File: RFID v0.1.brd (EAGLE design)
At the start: 87 x 53.3 mm, 32 parts, among them K1 G5LE, Q1 XTAL 16MHz, T1 BC817-40, U1 ARDUINOSPI-REFRENCE, U2 POWER-POD 5V0, U3 ATMEGA328P-MU, U4 POWER-POD 3V3

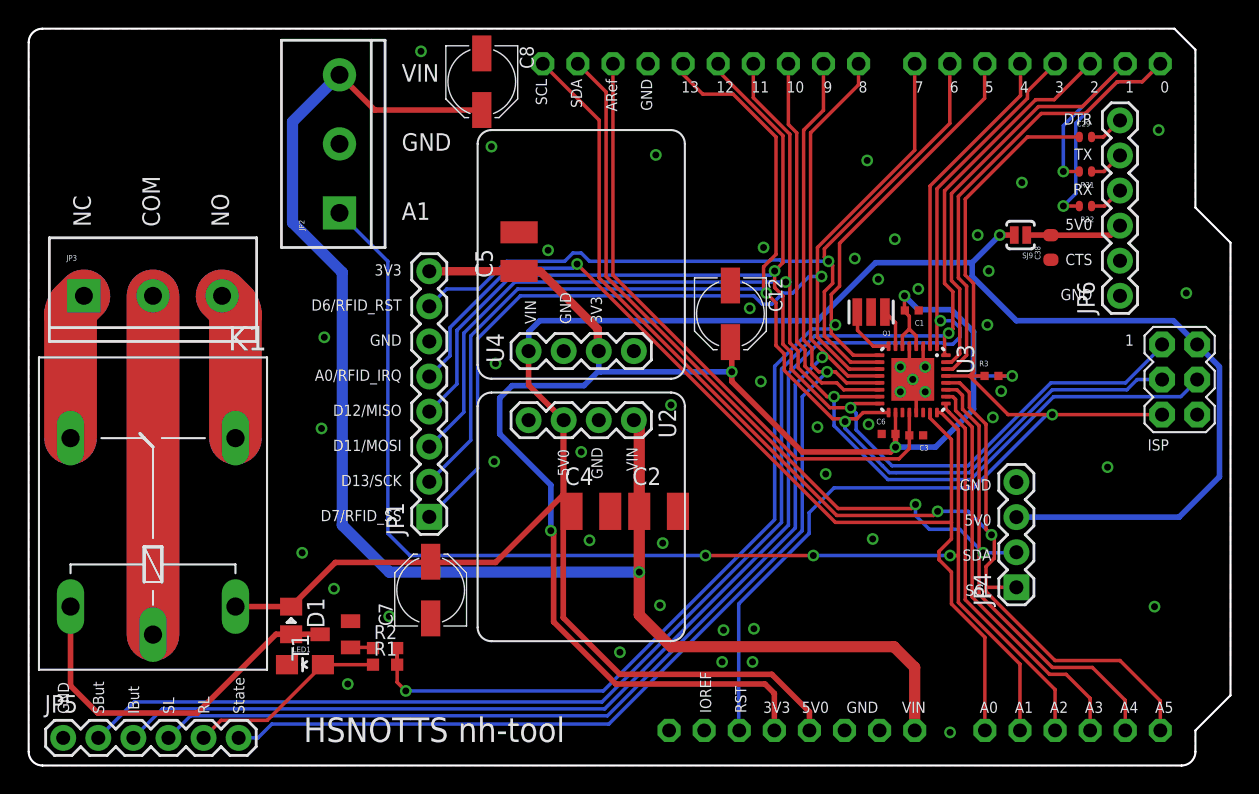
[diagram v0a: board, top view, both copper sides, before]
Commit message: Add early box design and some WIP board layout
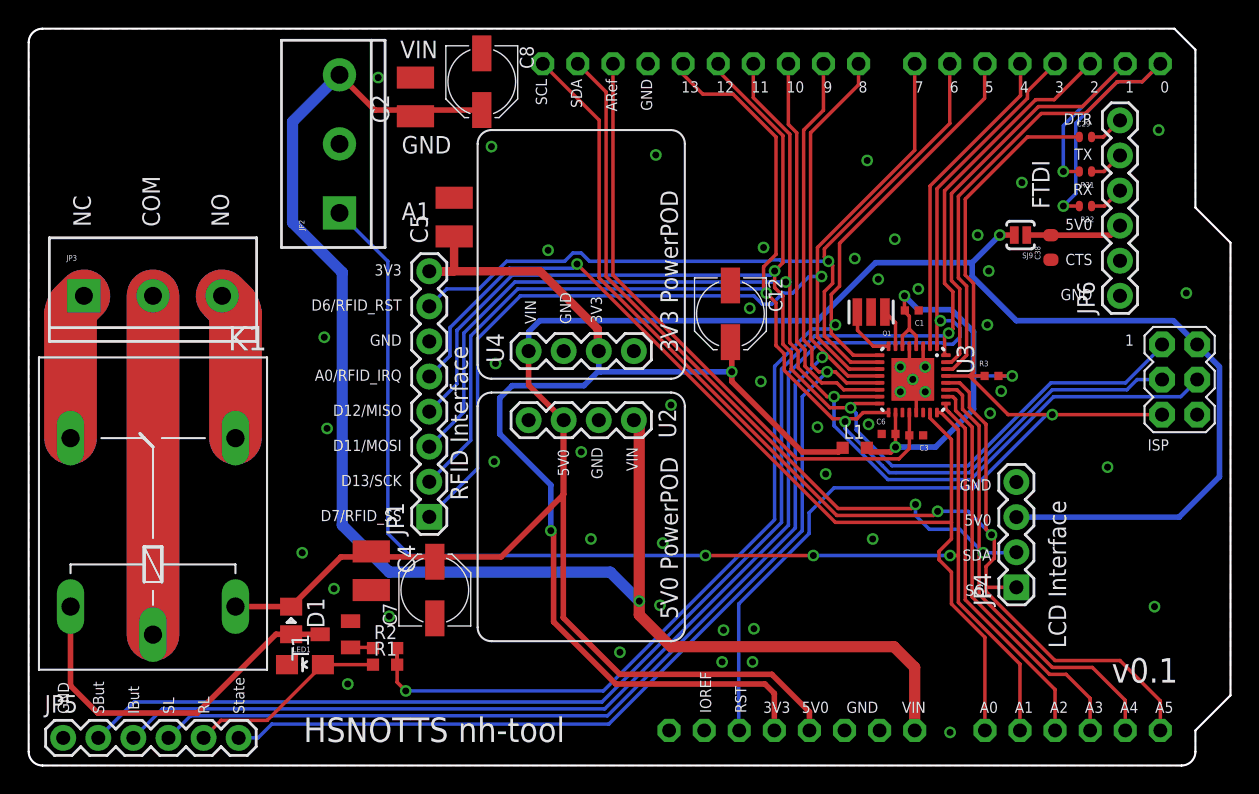
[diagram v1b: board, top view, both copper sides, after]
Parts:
- added L1: (no value), CISECO eaglecad designs:C0603K-SMALL
- moved C2 34.8 mm to (28.0, 48.4), turned to 90 degrees
- moved C4 16.5 mm to (24.8, 14.1), turned to 270 degrees
- moved C5 5.32 mm to (30.8, 39.7)
- moved C7 0.30 mm to (29.4, 12.7)
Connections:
- new net VCC: C1.2, C6.2, L1.2, R3.2, U3.18, U3.4, U3.6
- net 3V3: now also L1.1; no longer C1.2, C6.2, R3.2, U3.18, U3.4, U3.6
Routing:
- net VCC: track 0.00 -> 32.7 mm, vias 0 -> 3
- net 3V3: track 120.7 -> 90.8 mm, vias 5 -> 2
- net VIN: track 110.1 -> 111.0 mm
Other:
- board text added: "3V3 PowerPOD"
- board text added: "5V0 PowerPOD"
- board text added: "FTDI"
- board text added: "LCD Interface"
- board text added: "RFID Interface"
- board text added: "v0.1"
